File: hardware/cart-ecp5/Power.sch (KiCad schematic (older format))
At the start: 31 parts, among them U5 TPS2111A, U6 TLV62568DBV, U7 TLV62568DBV, U8 TLV73325PDBV

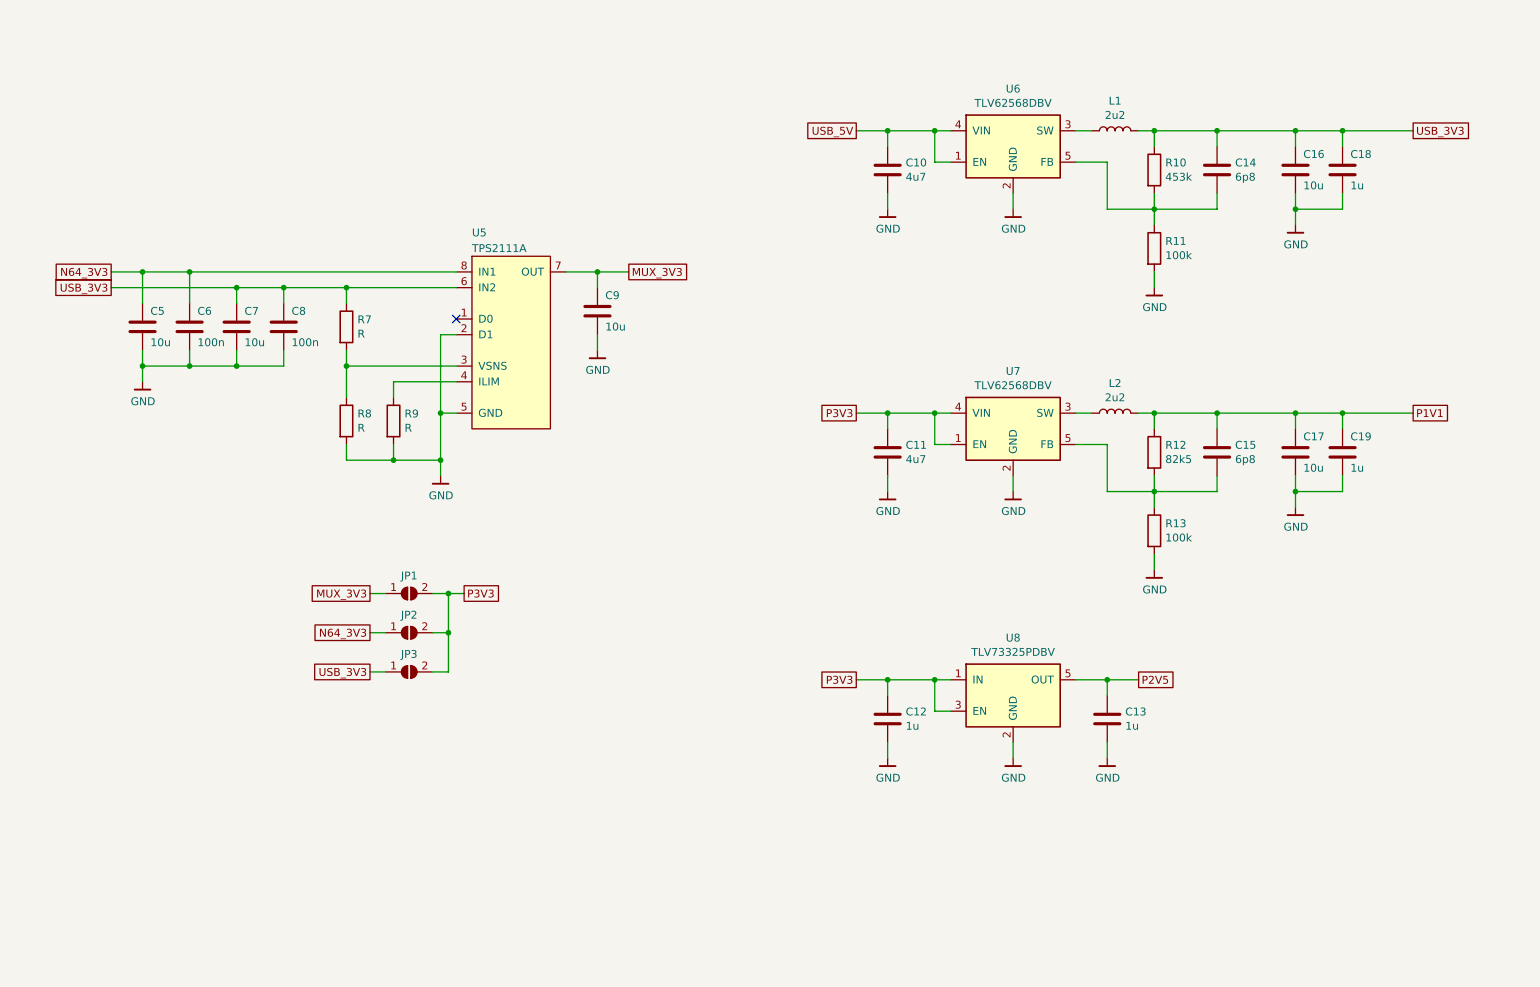
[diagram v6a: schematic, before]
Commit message: Add TPS2121 power mux to schematic and assign footprints
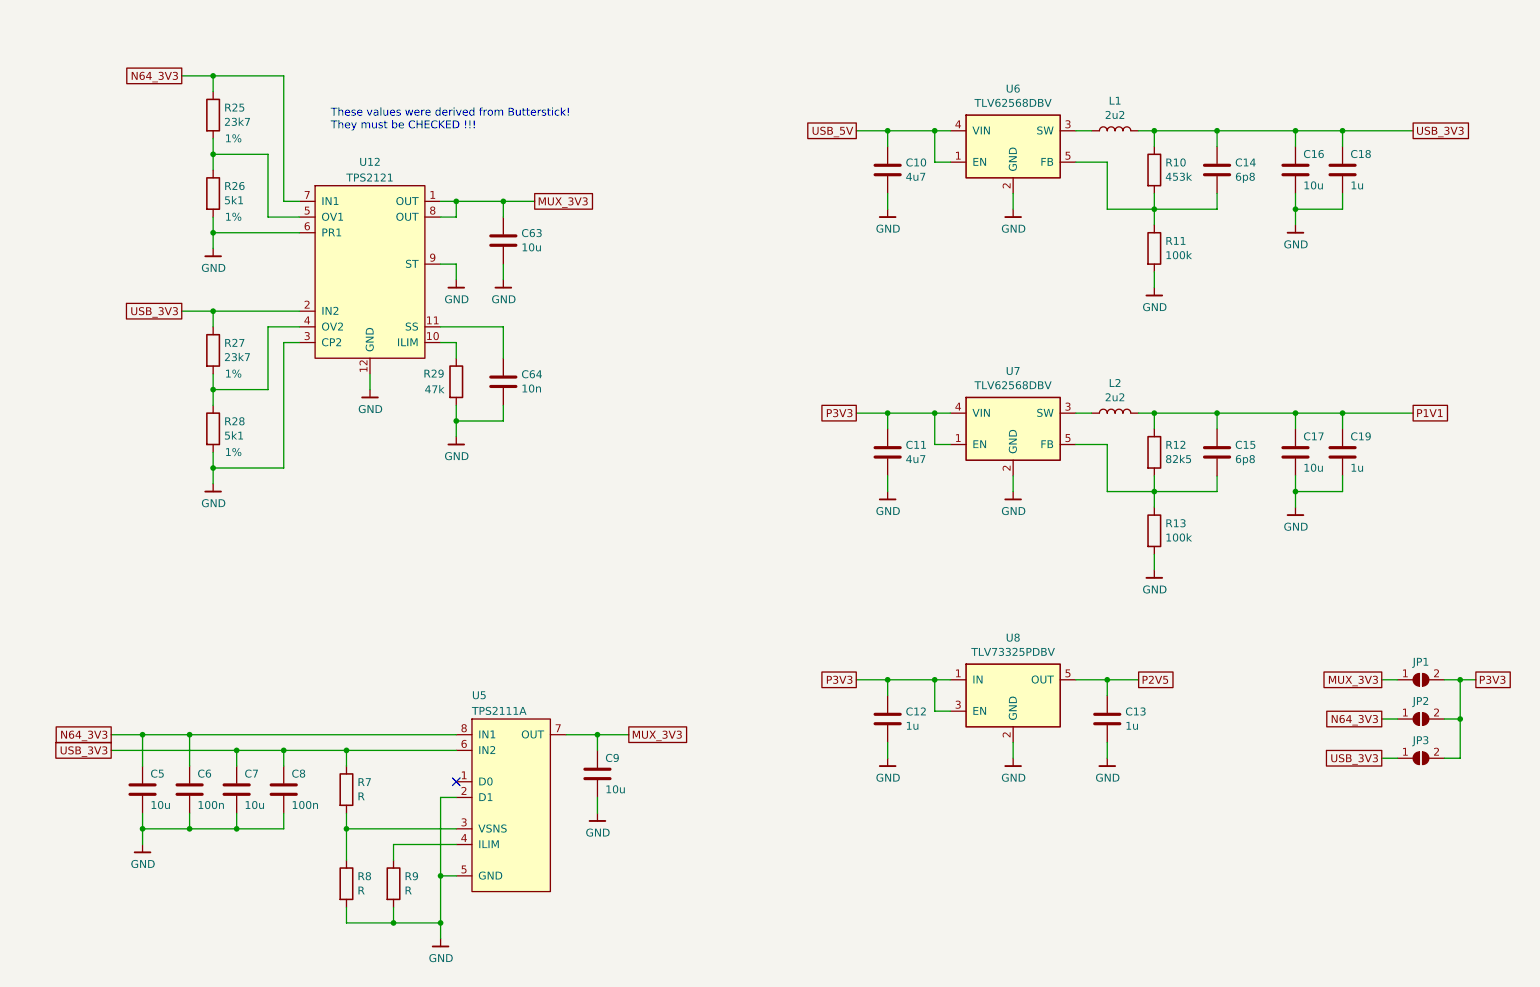
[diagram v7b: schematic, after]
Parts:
- added C63: 10u, Capacitor_SMD:C_0603_1608Metric, symbol Device:C
- added C64: 10n, Capacitor_SMD:C_0402_1005Metric, symbol Device:C
- added R25, R27: 23k7, Resistor_SMD:R_0402_1005Metric, symbol Device:R
- added R26, R28: 5k1, Resistor_SMD:R_0402_1005Metric, symbol Device:R
- added R29: 47k, Resistor_SMD:R_0402_1005Metric, symbol Device:R
- added U12: TPS2121, ng_package_qfn:Texas_VQFN-HR-12, symbol ng_pmic:TPS2121
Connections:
- net GND: now also C63.2, C64.2, R26.2, R28.2, R29.2, U12.12 (GND), U12.3 (CP2), U12.6 (PR1), U12.9 (ST)
- net MUX_3V3: now also C63.1, U12.1 (OUT), U12.8 (OUT)
- net N64_3V3: now also R25.1, U12.7 (IN1)
- net USB_3V3: now also R27.1, U12.2 (IN2)
- new net: R29.1, U12.10 (ILIM)
- new net: C64.1, U12.11 (SS)
- new net: R27.2, R28.1, U12.4 (OV2)
- new net: R25.2, R26.1, U12.5 (OV1)
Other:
- note added: "These values were derived from Butterstick!\nThey must be CHECKED !!!"
- moved on the sheet: C5, C6, C7, C8, C9, JP1, JP2, JP3, R7, R8, R9, U5

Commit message: Add a switching supply for a 1V8 rail
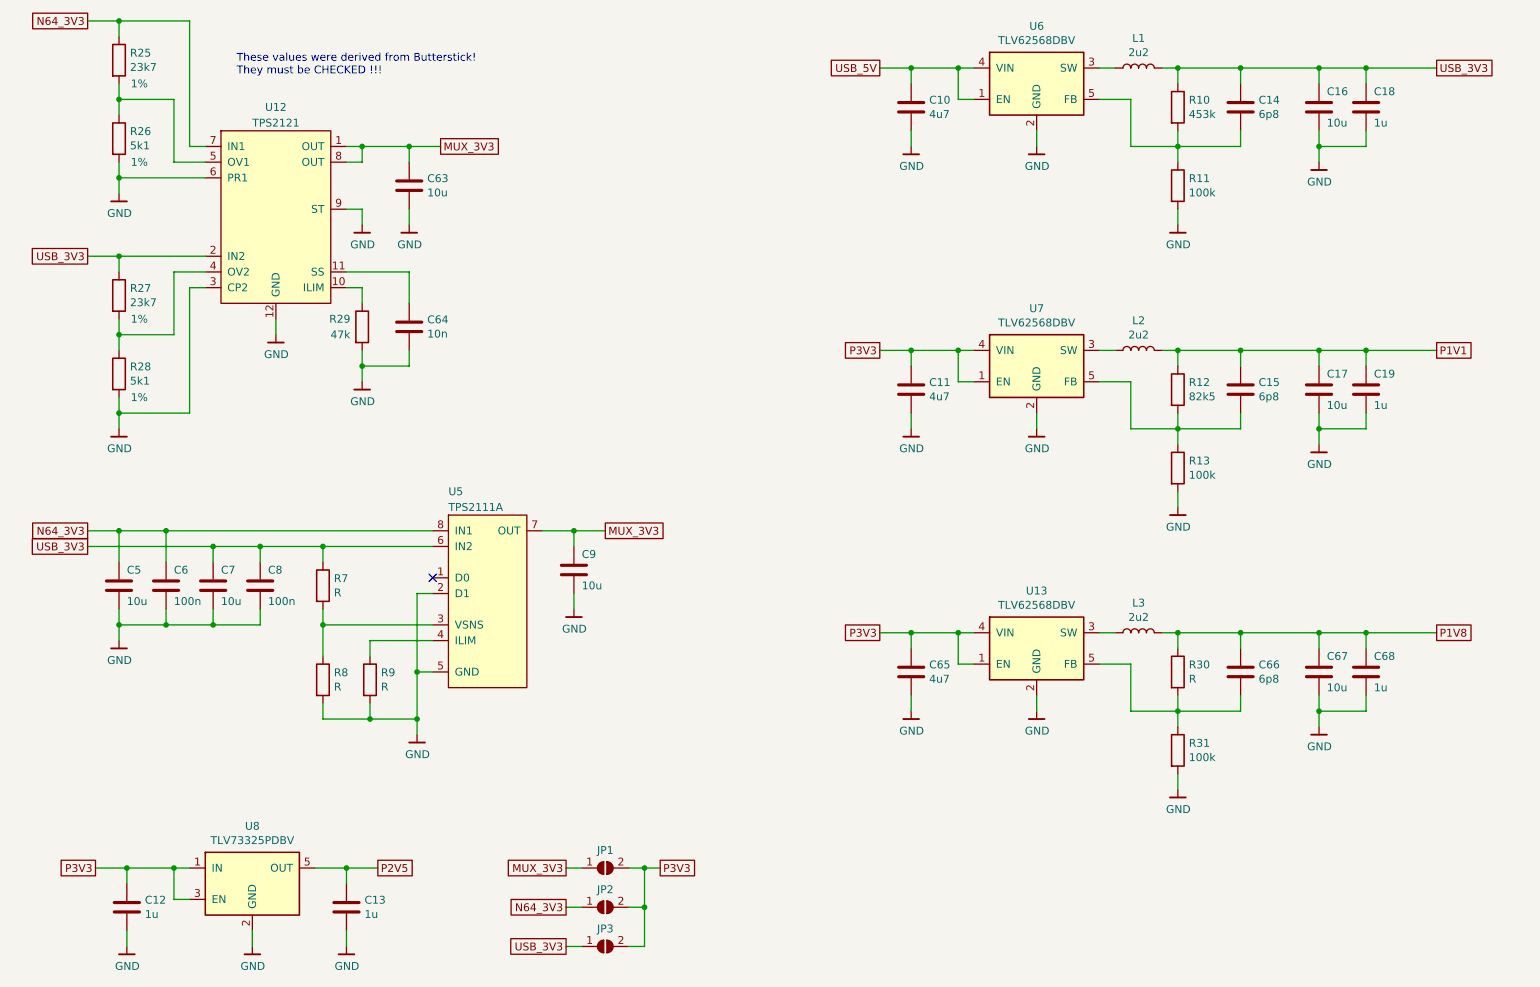
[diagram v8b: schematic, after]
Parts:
- added C65: 4u7, Capacitor_SMD:C_0402_1005Metric, symbol Device:C
- added C66: 6p8, Capacitor_SMD:C_0402_1005Metric, symbol Device:C
- added C67: 10u, Capacitor_SMD:C_0603_1608Metric, symbol Device:C
- added C68: 1u, Capacitor_SMD:C_0402_1005Metric, symbol Device:C
- added L3: 2u2, Inductor_SMD:L_0805_2012Metric, symbol Device:L
- added R30: R, Resistor_SMD:R_0402_1005Metric, symbol Device:R
- added R31: 100k, Resistor_SMD:R_0402_1005Metric, symbol Device:R
- added U13: TLV62568DBV, Package_TO_SOT_SMD:SOT-23-5, symbol ng_regulator:TLV62568DBV
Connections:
- net GND: now also C65.2, C67.2, C68.2, R31.2, U13.2 (GND)
- net P3V3: now also C65.1, U13.1 (EN), U13.4 (VIN)
- new net: L3.1, U13.3 (SW)
- new net: C66.2, R30.2, R31.1, U13.5 (FB)
- new net P1V8: C66.1, C67.1, C68.1, L3.2, R30.1
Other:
- moved on the sheet: C10, C11, C12, C13, C14, C15, C16, C17, C18, C19, C5, C6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
